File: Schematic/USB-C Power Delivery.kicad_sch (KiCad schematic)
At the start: 0 parts

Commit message: added sensors?
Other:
- note added: "## The Correct Flashing Process Here is the correct workflow: Generate Your Configuration: Use the TPS2575x Application Customization Tool from Texas Instruments to create the binary file (.bin) that contains all your desired settings. Program the EEPROM Separately: Connect the CAT24C512 EEPROM to your dedicated flasher or an Arduino. Do this before connecting it to the TPS25751. Connect power (V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"
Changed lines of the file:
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@@
 		)
+	)
+	(text "## The Correct Flashing Process\nHere is the correct workflow:\n\nGenerate Your Configuration: Use the TPS2575x Application Customization Tool from Texas Instruments to create the binary file (.bin) that contains all your desired settings.\n\nProgram the EEPROM Separately: Connect the CAT24C512 EEPROM to your dedicated flasher or an Arduino. Do this before connecting it to the TPS25751.\n\nConnect power (VCC), ground (GND), SDA, and SCL.\n\nUse the flasher's software to write the .bin file you generated onto the EEPROM.\n\nAssemble the Final Circuit: Once the EEPROM is successfully flashed, connect it to the I2Cc (the controller port) of the TPS25751.\n\nNow, when you power on your circuit, the TPS25751 will use its I2Cc port to automatically read the settings you loaded onto the EEPROM and will configure itself correctly."
+		(exclude_from_sim no)
+		(at 94.996 179.832 0)
+		(effects
+			(font
+				(size 1.143 1.143)
+			)
+		)
+	)
+	(junction
+		(at 107.95 128.27)
+		(diameter 0)
+		(color 0 0 0 0)
 	)
 	(junction
@@
 	(wire
 		(pts
-			(xy 130.81 34.29) (xy 133.35 34.29)
-		)
-		(stroke
-			(width 0)
-			(type default)
-		)
-	)
-	(wire
-		(pts
 			(xy 71.12 69.85) (xy 71.12 43.18)
 		)
@@
 	(wire
 		(pts
-			(xy 104.14 128.27) (xy 124.46 128.27)
+			(xy 104.14 128.27) (xy 107.95 128.27)
 		)
 		(stroke
@@
 	(wire
 		(pts
+			(xy 107.95 128.27) (xy 124.46 128.27)
+		)
+		(stroke
+			(width 0)
+			(type default)
+		)
+	)
+	(wire
+		(pts
 			(xy 198.12 71.12) (xy 224.79 71.12)
 		)
@@
 	(wire
 		(pts
+			(xy 130.81 34.29) (xy 132.08 34.29)
+		)
+		(stroke
+			(width 0)
+			(type default)
+		)
+	)
+	(wire
+		(pts
 			(xy 148.59 38.1) (xy 163.83 38.1)
 		)
@@
 	(wire
 		(pts
+			(xy 107.95 128.27) (xy 107.95 133.35)
+		)
+		(stroke
+			(width 0)
+			(type default)
+		)
+	)
+	(wire
+		(pts
 			(xy 198.12 73.66) (xy 224.79 73.66)
+		)
+		(stroke
+			(width 0)
+			(type default)
+		)
+	)
+	(wire
+		(pts
+			(xy 107.95 133.35) (xy 111.76 133.35)
 		)
 		(stroke
@@
 			)
 			(justify right bottom)
+		)
+	)
+	(hierarchical_label "P5V0"
+		(shape output)
+		(at 111.76 133.35 0)
+		(effects
+			(font
+				(size 1.27 1.27)
+			)
+			(justify left)
+		)
+	)
+	(hierarchical_label "SDA"
+		(shape input)
+		(at 148.59 40.64 180)
+		(effects
+			(font
+				(size 1.27 1.27)
+			)
+			(justify right)
 		)
 	)
@@
 		)
 	)
-	(hierarchical_label "SDA"
-		(shape output)
-		(at 148.59 40.64 180)
-		(effects
-			(font
-				(size 1.27 1.27)
-			)
-			(justify right)
-		)
-	)
 	(hierarchical_label "SCL"
-		(shape output)
+		(shape input)
 		(at 148.59 38.1 180)
 		(effects
@@
 	(hierarchical_label "LDO_3V3"
 		(shape output)
-		(at 133.35 34.29 0)
+		(at 132.08 34.29 0)
 		(effects
 			(font
@@
 		)
 		(instances
-			(project "Project-Star"
+			(project "STAR"
 				(path "/fc8533bc-25dd-4c20-9b4c-ffebebd6739b/ec72a35b-e7f2-4422-8859-60e9fb848154"
 					(page "16")
@@
 		)
 		(instances
-			(project "Project-Star"
+			(project "STAR"
 				(path "/fc8533bc-25dd-4c20-9b4c-ffebebd6739b/ec72a35b-e7f2-4422-8859-60e9fb848154"
 					(page "17")
@@
 		)
 		(instances
-			(project "Project-Star"
+			(project "STAR"
 				(path "/fc8533bc-25dd-4c20-9b4c-ffebebd6739b/ec72a35b-e7f2-4422-8859-60e9fb848154"
 					(page "19")
@@
 		)
 		(instances
-			(project "Project-Star"
+			(project "STAR"
 				(path "/fc8533bc-25dd-4c20-9b4c-ffebebd6739b/ec72a35b-e7f2-4422-8859-60e9fb848154"
 					(page "14")
@@
 		)
 		(instances
-			(project "Project-Star"
+			(project "STAR"
 				(path "/fc8533bc-25dd-4c20-9b4c-ffebebd6739b/ec72a35b-e7f2-4422-8859-60e9fb848154"
 					(page "15")
@@
 		)
 		(instances
-			(project "Project-Star"
+			(project "STAR"
 				(path "/fc8533bc-25dd-4c20-9b4c-ffebebd6739b/ec72a35b-e7f2-4422-8859-60e9fb848154"
 					(page "18")
@@
 		)
 		(instances
-			(project "Project-Star"
+			(project "STAR"
 				(path "/fc8533bc-25dd-4c20-9b4c-ffebebd6739b/ec72a35b-e7f2-4422-8859-60e9fb848154"
 					(page "13")

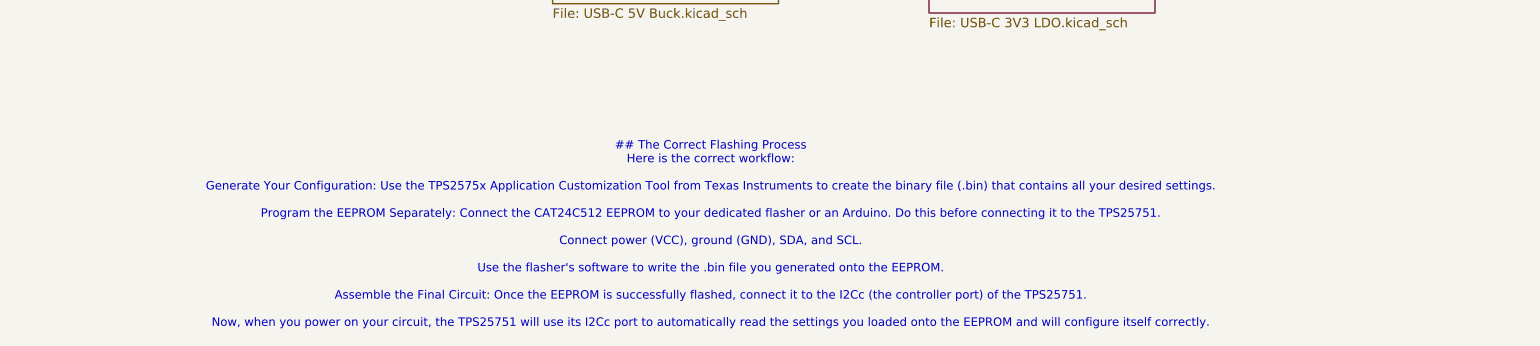
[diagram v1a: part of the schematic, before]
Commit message: Added MCU
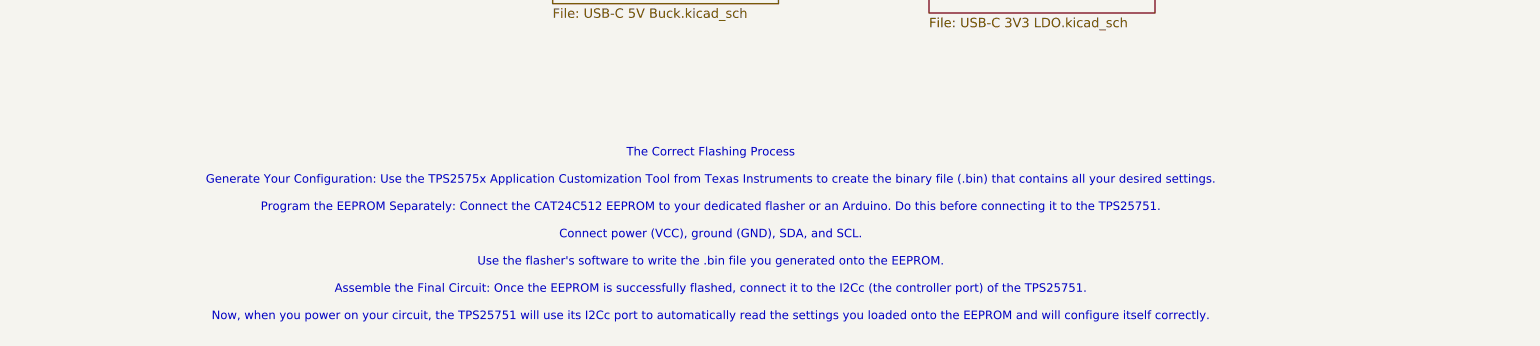
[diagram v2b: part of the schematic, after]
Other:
- note added: "The Correct Flashing Process Generate Your Configuration: Use the TPS2575x Application Customization Tool from Texas Instruments to create the binary file (.bin) that contains all your desired settings. Program the EEPROM Separately: Connect the CAT24C512 EEPROM to your dedicated flasher or an Arduino. Do this before connecting it to the TPS25751. Connect power (VCC), ground (GND), SDA, and SCL. 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"
- note removed: "## The Correct Flashing Process Here is the correct workflow: Generate Your Configuration: Use the TPS2575x Application Customization Tool from Texas Instruments to create the binary file (.bin) that contains all your desired settings. Program the EEPROM Separately: Connect the CAT24C512 EEPROM to your dedicated flasher or an Arduino. Do this before connecting it to the TPS25751. Connect power (V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"
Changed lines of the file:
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@@
 		)
 	)
-	(text "## The Correct Flashing Process\nHere is the correct workflow:\n\nGenerate Your Configuration: Use the TPS2575x Application Customization Tool from Texas Instruments to create the binary file (.bin) that contains all your desired settings.\n\nProgram the EEPROM Separately: Connect the CAT24C512 EEPROM to your dedicated flasher or an Arduino. Do this before connecting it to the TPS25751.\n\nConnect power (VCC), ground (GND), SDA, and SCL.\n\nUse the flasher's software to write the .bin file you generated onto the EEPROM.\n\nAssemble the Final Circuit: Once the EEPROM is successfully flashed, connect it to the I2Cc (the controller port) of the TPS25751.\n\nNow, when you power on your circuit, the TPS25751 will use its I2Cc port to automatically read the settings you loaded onto the EEPROM and will configure itself correctly."
+	(text "The Correct Flashing Process\n\nGenerate Your Configuration: Use the TPS2575x Application Customization Tool from Texas Instruments to create the binary file (.bin) that contains all your desired settings.\n\nProgram the EEPROM Separately: Connect the CAT24C512 EEPROM to your dedicated flasher or an Arduino. Do this before connecting it to the TPS25751.\n\nConnect power (VCC), ground (GND), SDA, and SCL.\n\nUse the flasher's software to write the .bin file you generated onto the EEPROM.\n\nAssemble the Final Circuit: Once the EEPROM is successfully flashed, connect it to the I2Cc (the controller port) of the TPS25751.\n\nNow, when you power on your circuit, the TPS25751 will use its I2Cc port to automatically read the settings you loaded onto the EEPROM and will configure itself correctly."
 		(exclude_from_sim no)
 		(at 94.996 179.832 0)
@@
 			(project "STAR"
 				(path "/fc8533bc-25dd-4c20-9b4c-ffebebd6739b/ec72a35b-e7f2-4422-8859-60e9fb848154"
-					(page "16")
+					(page "21")
 				)
 			)
@@
 			(project "STAR"
 				(path "/fc8533bc-25dd-4c20-9b4c-ffebebd6739b/ec72a35b-e7f2-4422-8859-60e9fb848154"
-					(page "17")
+					(page "22")
 				)
 			)
@@
 			(project "STAR"
 				(path "/fc8533bc-25dd-4c20-9b4c-ffebebd6739b/ec72a35b-e7f2-4422-8859-60e9fb848154"
-					(page "19")
+					(page "23")
 				)
 			)
@@
 			(project "STAR"
 				(path "/fc8533bc-25dd-4c20-9b4c-ffebebd6739b/ec72a35b-e7f2-4422-8859-60e9fb848154"
-					(page "14")
+					(page "19")
 				)
 			)
@@
 			(project "STAR"
 				(path "/fc8533bc-25dd-4c20-9b4c-ffebebd6739b/ec72a35b-e7f2-4422-8859-60e9fb848154"
-					(page "15")
+					(page "20")
 				)
 			)
@@
 			(project "STAR"
 				(path "/fc8533bc-25dd-4c20-9b4c-ffebebd6739b/ec72a35b-e7f2-4422-8859-60e9fb848154"
-					(page "18")
+					(page "24")
 				)
 			)
@@
 			(project "STAR"
 				(path "/fc8533bc-25dd-4c20-9b4c-ffebebd6739b/ec72a35b-e7f2-4422-8859-60e9fb848154"
-					(page "13")
-				)
-			)
+					(page "18")
+				)
+			)
